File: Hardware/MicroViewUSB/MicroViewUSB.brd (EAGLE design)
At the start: 27.9 x 20.3 mm, 28 parts, among them J1 MICROVIEW-16ND, Q1 2N7002PW, U1 FT231XS

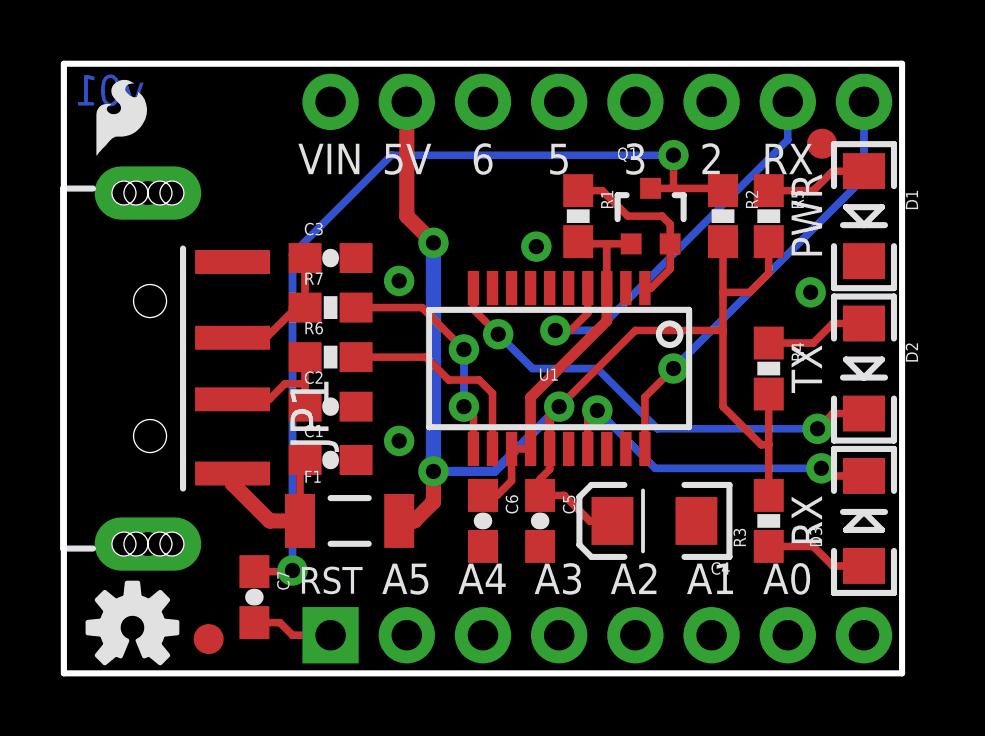
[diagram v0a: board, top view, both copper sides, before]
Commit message: Moving USB connector position (MVUSB v02)
Also added silk to indicate polarity of MV.
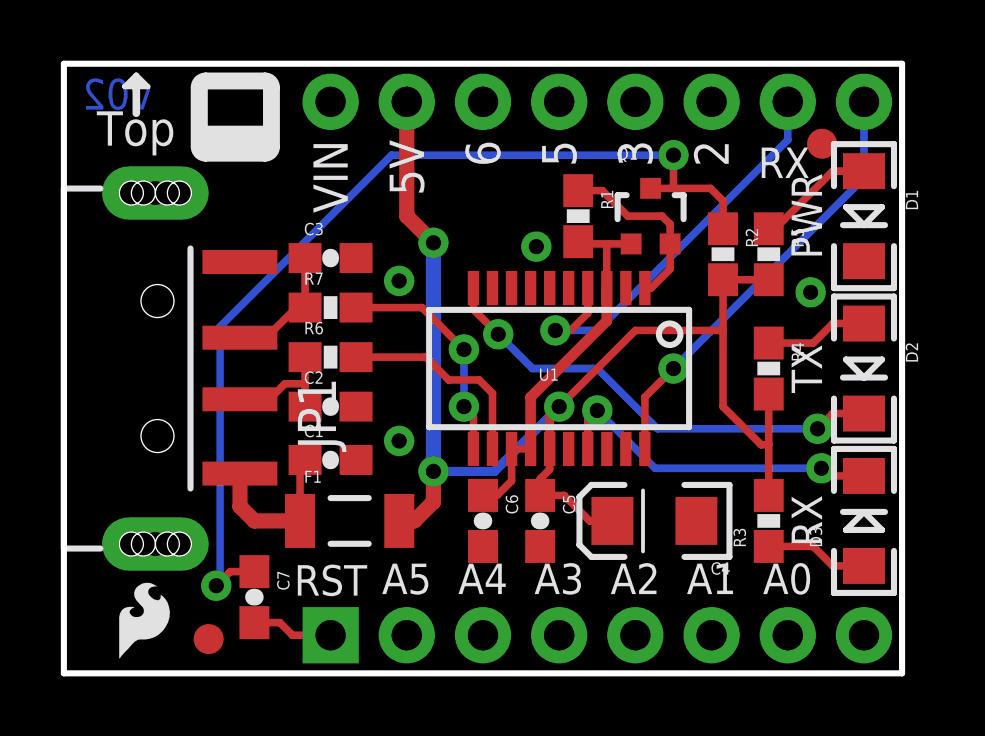
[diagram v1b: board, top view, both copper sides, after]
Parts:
- moved LOGO2 23.5 mm to (24.1, 10.2), flipped to the bottom
- moved LOGO1 16.8 mm to (1.52, 0.13)
- moved JP1 2.54 mm to (0.00, 10.2)
- moved LOGO3 1.27 mm to (21.6, 10.2)
- moved R2 1.27 mm to (22.0, 14.0)
- moved R5 1.27 mm to (23.5, 14.0)
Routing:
- net DTR: track 29.4 -> 32.3 mm
- net 5V: track 46.5 -> 43.9 mm
- net N$1: track 3.44 -> 3.97 mm
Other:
- board text added: "Top"
- board text added: "v02"
- board text removed: "v01"
